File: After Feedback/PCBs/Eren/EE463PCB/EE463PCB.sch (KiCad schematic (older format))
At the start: 16 parts, among them J1 Conn_01x03, J2 Conn_01x02, Q1 IPD50R650CE, U1 HV9961LG-G

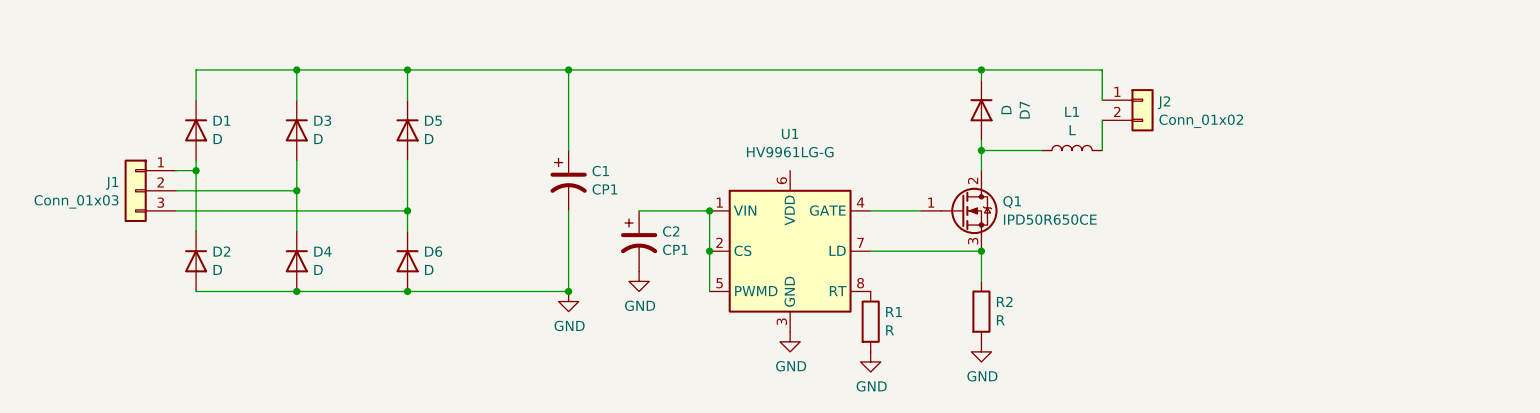
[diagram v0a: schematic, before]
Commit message: New components file is updated and PCB schematic is also updated
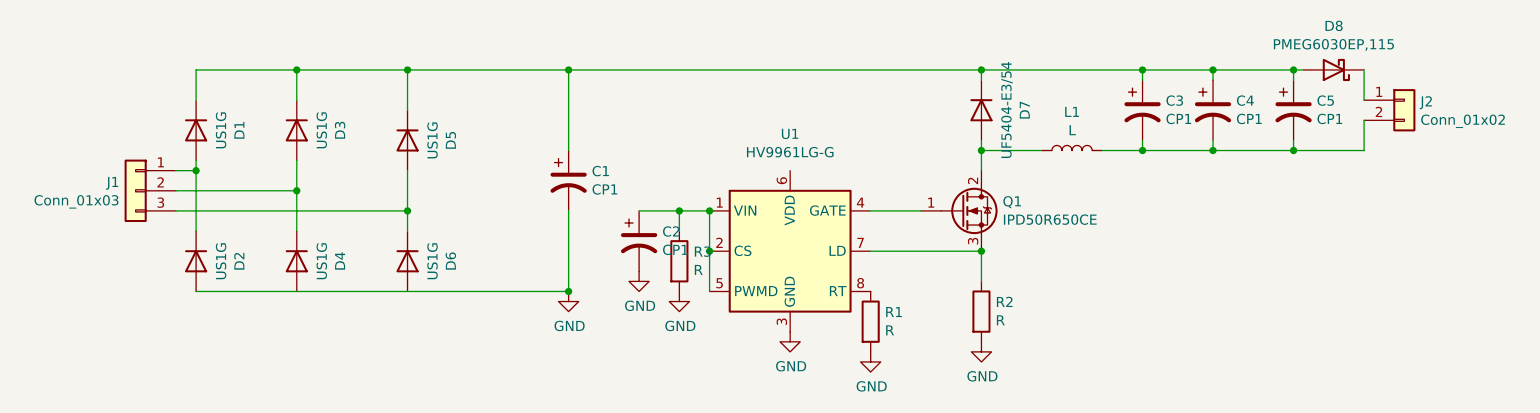
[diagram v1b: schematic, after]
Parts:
- removed D1, D2, D3, D4, D5, D6, D7: D, symbol Device:D
- added C3, C4, C5: CP1, Capacitor_SMD:C_0201_0603Metric, symbol Device:CP1
- added D1, D2, D3, D4, D5, D6: US1G, Diode_SMD:D_SMA, symbol Diode:US1G
- added D7: UF5404-E3/54, Diode_THT:D_DO-201AD_P15.24mm_Horizontal, symbol Diode:UF5404
- added D8: PMEG6030EP,115, Diode_SMD:D_SOD-128, symbol Diode:PMEG6030EP
- added R3: R, Resistor_SMD:R_4020_10251Metric, symbol Device:R
- C1: footprint (none) -> Capacitor_THT:CP_Axial_L25.0mm_D10.0mm_P30.00mm_Horizontal
- C2: footprint (none) -> Capacitor_SMD:C_0402_1005Metric
- J1: footprint (none) -> Connector_PinSocket_2.54mm:PinSocket_1x03_P2.54mm_Vertical
- J2: footprint (none) -> Connector_PinSocket_1.00mm:PinSocket_1x02_P1.00mm_Vertical
- L1: footprint (none) -> Inductor_THT:L_Radial_D28.0mm_P29.20mm
- R1, R2: footprint (none) -> Resistor_SMD:R_4020_10251Metric
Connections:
- net GND: now also D2.2 (A), R3.2
- net at C2.1, U1.1 (VIN), U1.2 (CS)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: now also R3.1
- net at J2.1 (Pin_1): now also D8.1 (K); no longer C1.1
- net at J2.2 (Pin_2), L1.2: now also C3.2, C4.2, C5.2
- net at J1.3 (Pin_3): now also D5.2 (A), D6.1 (K)
- net at J1.2 (Pin_2): now also D3.2 (A), D4.1 (K)
- net at J1.1 (Pin_1): now also D1.2 (A), D2.1 (K)
- net at L1.1, Q1.2 (D): now also D7.2 (A)
- new net: C1.1, C3.1, C4.1, C5.1, D1.1 (K), D3.1 (K), D5.1 (K), D7.1 (K), D8.2 (A)
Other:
- moved on the sheet: J2
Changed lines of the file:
@@
 F 0 "R1" H 6920 4746 50  0000 L CNN
 F 1 "R" H 6920 4655 50  0000 L CNN
-F 2 "" V 6780 4700 50  0001 C CNN
+F 2 "Resistor_SMD:R_4020_10251Metric" V 6780 4700 50  0001 C CNN
 F 3 "~" H 6850 4700 50  0001 C CNN
 	1    6850 4700
@@
 F 0 "R2" H 7470 4696 50  0000 L CNN
 F 1 "R" H 7470 4605 50  0000 L CNN
-F 2 "" V 7330 4650 50  0001 C CNN
+F 2 "Resistor_SMD:R_4020_10251Metric" V 7330 4650 50  0001 C CNN
 F 3 "~" H 7400 4650 50  0001 C CNN
 	1    7400 4650
@@
 F 0 "C2" H 5815 4346 50  0000 L CNN
 F 1 "CP1" H 5815 4255 50  0000 L CNN
-F 2 "" H 5700 4300 50  0001 C CNN
+F 2 "Capacitor_SMD:C_0402_1005Metric" H 5700 4300 50  0001 C CNN
 F 3 "~" H 5700 4300 50  0001 C CNN
 	1    5700 4300
@@
 Connection ~ 6050 4350
 Wire Wire Line
-	6050 4150 5700 4150
+	6050 4150 5900 4150
 Connection ~ 6050 4150
-$Comp
-L Device:D D7
-U 1 1 5FF92910
-P 7400 3650
-F 0 "D7" H 7400 3867 50  0000 C CNN
-F 1 "D" H 7400 3776 50  0000 C CNN
-F 2 "" H 7400 3650 50  0001 C CNN
-F 3 "~" H 7400 3650 50  0001 C CNN
-	1    7400 3650
-	0    1    1    0
-$EndComp
 Wire Wire Line
 	7400 3950 7400 3850
@@
 F 0 "L1" V 8040 3850 50  0000 C CNN
 F 1 "L" V 7949 3850 50  0000 C CNN
-F 2 "" H 7850 3850 50  0001 C CNN
+F 2 "Inductor_THT:L_Radial_D28.0mm_P29.20mm" H 7850 3850 50  0001 C CNN
 F 3 "~" H 7850 3850 50  0001 C CNN
 	1    7850 3850
@@
 F 0 "C1" H 5465 4046 50  0000 L CNN
 F 1 "CP1" H 5465 3955 50  0000 L CNN
-F 2 "" H 5350 4000 50  0001 C CNN
+F 2 "Capacitor_THT:CP_Axial_L25.0mm_D10.0mm_P30.00mm_Horizontal" H 5350 4000 50  0001 C CNN
 F 3 "~" H 5350 4000 50  0001 C CNN
 	1    5350 4000
@@
 Wire Wire Line
 	7400 3850 7400 3800
-Wire Wire Line
-	7400 3450 8000 3450
-Connection ~ 7400 3450
 $Comp
 L Connector_Generic:Conn_01x02 J2
 U 1 1 5FF87428
-P 8200 3600
-F 0 "J2" H 8280 3592 50  0000 L CNN
-F 1 "Conn_01x02" H 8280 3501 50  0000 L CNN
-F 2 "" H 8200 3600 50  0001 C CNN
-F 3 "~" H 8200 3600 50  0001 C CNN
-	1    8200 3600
-	1    0    0    -1
-$EndComp
-Wire Wire Line
-	8000 3850 8000 3700
-Wire Wire Line
-	8000 3450 8000 3600
-$Comp
-L Device:D D5
-U 1 1 5FF893A3
-P 4550 3750
-F 0 "D5" V 4504 3830 50  0000 L CNN
-F 1 "D" V 4595 3830 50  0000 L CNN
-F 2 "" H 4550 3750 50  0001 C CNN
-F 3 "~" H 4550 3750 50  0001 C CNN
-	1    4550 3750
-	0    1    1    0
-$EndComp
-$Comp
-L Device:D D3
-U 1 1 5FF8B368
-P 4000 3750
-F 0 "D3" V 3954 3830 50  0000 L CNN
-F 1 "D" V 4045 3830 50  0000 L CNN
-F 2 "" H 4000 3750 50  0001 C CNN
-F 3 "~" H 4000 3750 50  0001 C CNN
-	1    4000 3750
-	0    1    1    0
-$EndComp
-$Comp
-L Device:D D1
-U 1 1 5FF8B8EB
-P 3500 3750
-F 0 "D1" V 3454 3830 50  0000 L CNN
-F 1 "D" V 3545 3830 50  0000 L CNN
-F 2 "" H 3500 3750 50  0001 C CNN
-F 3 "~" H 3500 3750 50  0001 C CNN
-	1    3500 3750
-	0    1    1    0
-$EndComp
-$Comp
-L Device:D D6
-U 1 1 5FF8D494
-P 4550 4400
-F 0 "D6" V 4504 4480 50  0000 L CNN
-F 1 "D" V 4595 4480 50  0000 L CNN
-F 2 "" H 4550 4400 50  0001 C CNN
-F 3 "~" H 4550 4400 50  0001 C CNN
-	1    4550 4400
-	0    1    1    0
-$EndComp
-$Comp
-L Device:D D4
-U 1 1 5FF8D49A
-P 4000 4400
-F 0 "D4" V 3954 4480 50  0000 L CNN
-F 1 "D" V 4045 4480 50  0000 L CNN
-F 2 "" H 4000 4400 50  0001 C CNN
-F 3 "~" H 4000 4400 50  0001 C CNN
-	1    4000 4400
-	0    1    1    0
-$EndComp
-$Comp
-L Device:D D2
-U 1 1 5FF8D4A0
-P 3500 4400
-F 0 "D2" V 3454 4480 50  0000 L CNN
-F 1 "D" V 3545 4480 50  0000 L CNN
-F 2 "" H 3500 4400 50  0001 C CNN
-F 3 "~" H 3500 4400 50  0001 C CNN
-	1    3500 4400
-	0    1    1    0
+P 9500 3600
+F 0 "J2" H 9580 3592 50  0000 L CNN
+F 1 "Conn_01x02" H 9580 3501 50  0000 L CNN
+F 2 "Connector_PinSocket_1.00mm:PinSocket_1x02_P1.00mm_Vertical" H 9500 3600 50  0001 C CNN
+F 3 "~" H 9500 3600 50  0001 C CNN
+	1    9500 3600
+	1    0    0    -1
 $EndComp
 Wire Wire Line
@@
 Wire Wire Line
 	5350 3450 4550 3450
-Wire Wire Line
-	4550 3450 4550 3600
 Connection ~ 5350 3450
-Wire Wire Line
-	4550 3450 4000 3450
-Wire Wire Line
-	4000 3450 4000 3600
 Connection ~ 4550 3450
 Wire Wire Line
-	4000 3450 3500 3450
-Wire Wire Line
 	3500 3450 3500 3600
-Connection ~ 4000 3450
 Wire Wire Line
 	3500 4250 3500 3950
 Wire Wire Line
-	3500 4550 4000 4550
-Wire Wire Line
-	4000 4550 4550 4550
-Connection ~ 4000 4550
-Wire Wire Line
-	4550 4550 5350 4550
-Wire Wire Line
 	5350 4550 5350 4150
-Connection ~ 4550 4550
 $Comp
 L Connector_Generic:Conn_01x03 J1
@@
 F 0 "J1" H 3280 4092 50  0000 L CNN
 F 1 "Conn_01x03" H 3280 4001 50  0000 L CNN
-F 2 "" H 3200 4050 50  0001 C CNN
+F 2 "Connector_PinSocket_2.54mm:PinSocket_1x03_P2.54mm_Vertical" H 3200 4050 50  0001 C CNN
 F 3 "~" H 3200 4050 50  0001 C CNN
 	1    3200 4050
@@
 	4000 4050 4000 4250
 Wire Wire Line
-	4550 3900 4550 4150
-Wire Wire Line
 	3400 4150 4550 4150
-Connection ~ 4550 4150
 Wire Wire Line
 	4550 4150 4550 4250
@@
 $EndComp
 Connection ~ 5350 4550
+$Comp
+L Device:R R3
+U 1 1 5FF9D255
+P 5900 4400
+F 0 "R3" H 5970 4446 50  0000 L CNN
+F 1 "R" H 5970 4355 50  0000 L CNN
+F 2 "Resistor_SMD:R_4020_10251Metric" V 5830 4400 50  0001 C CNN
+F 3 "~" H 5900 4400 50  0001 C CNN
+	1    5900 4400
+	1    0    0    -1
+$EndComp
+Wire Wire Line
+	5900 4250 5900 4150
+Connection ~ 5900 4150
+Wire Wire Line
+	5900 4150 5700 4150
+$Comp
+L power:GND #PWR06
+U 1 1 5FF9E138
+P 5900 4550
+F 0 "#PWR06" H 5900 4300 50  0001 C CNN
+F 1 "GND" H 5905 4377 50  0000 C CNN
+F 2 "" H 5900 4550 50  0001 C CNN
+F 3 "" H 5900 4550 50  0001 C CNN
+	1    5900 4550
+	1    0    0    -1
+$EndComp
+$Comp
+L Device:CP1 C3
+U 1 1 5FFA0F5C
+P 8200 3650
+F 0 "C3" H 8315 3696 50  0000 L CNN
+F 1 "CP1" H 8315 3605 50  0000 L CNN
+F 2 "Capacitor_SMD:C_0201_0603Metric" H 8200 3650 50  0001 C CNN
+F 3 "~" H 8200 3650 50  0001 C CNN
+	1    8200 3650
+	1    0    0    -1
+$EndComp
+Wire Wire Line
+	8200 3450 8200 3500
+Wire Wire Line
+	8200 3800 8200 3850
+Wire Wire Line
+	8200 3850 8000 3850
+Connection ~ 8200 3850
+$Comp
+L Device:CP1 C4
+U 1 1 5FFB0889
+P 8550 3650
+F 0 "C4" H 8665 3696 50  0000 L CNN
+F 1 "CP1" H 8665 3605 50  0000 L CNN
+F 2 "Capacitor_SMD:C_0201_0603Metric" H 8550 3650 50  0001 C CNN
+F 3 "~" H 8550 3650 50  0001 C CNN
+	1    8550 3650
+	1    0    0    -1
+$EndComp
+$Comp
+L Device:CP1 C5
+U 1 1 5FFB13E8
+P 8950 3650
+F 0 "C5" H 9065 3696 50  0000 L CNN
+F 1 "CP1" H 9065 3605 50  0000 L CNN
+F 2 "Capacitor_SMD:C_0201_0603Metric" H 8950 3650 50  0001 C CNN
+F 3 "~" H 8950 3650 50  0001 C CNN
+	1    8950 3650
+	1    0    0    -1
+$EndComp
+Wire Wire Line
+	8550 3450 8550 3500
+Wire Wire Line
+	8200 3450 8550 3450
+Wire Wire Line
+	8550 3450 8950 3450
+Wire Wire Line
+	8950 3450 8950 3500
+Connection ~ 8550 3450
+Wire Wire Line
+	8550 3800 8550 3850
+Wire Wire Line
+	8200 3850 8550 3850
+Wire Wire Line
+	8950 3800 8950 3850
+Wire Wire Line
+	8950 3850 8550 3850
+Connection ~ 8550 3850
+Wire Wire Line
+	9300 3700 9300 3850
+Wire Wire Line
+	9300 3850 8950 3850
+Connection ~ 8950 3850
+$Comp
+L Diode:US1G D1
+U 1 1 5FFBE7C3
+P 3500 3750
+F 0 "D1" H 3500 3967 50  0000 C CNN
+F 1 "US1G" H 3500 3876 50  0000 C CNN
+F 2 "Diode_SMD:D_SMA" H 3500 3575 50  0001 C CNN
+F 3 "https://www.diodes.com/assets/Datasheets/ds16008.pdf" H 3500 3750 50  0001 C CNN
+	1    3500 3750
+	0    1    1    0
+$EndComp
+Wire Wire Line
+	3500 3450 4000 3450
+Wire Wire Line
+	3500 4550 5350 4550
+$Comp
+L Diode:US1G D3
+U 1 1 5FFC5787
+P 4000 3750
+F 0 "D3" H 4000 3967 50  0000 C CNN
+F 1 "US1G" H 4000 3876 50  0000 C CNN
+F 2 "Diode_SMD:D_SMA" H 4000 3575 50  0001 C CNN
+F 3 "https://www.diodes.com/assets/Datasheets/ds16008.pdf" H 4000 3750 50  0001 C CNN
+	1    4000 3750
+	0    1    1    0
+$EndComp
+Wire Wire Line
+	4550 3450 4550 3650
+Wire Wire Line
+	4000 3600 4000 3450
+Connection ~ 4000 3450
+Wire Wire Line
+	4000 3450 4550 3450
+$Comp
+L Diode:US1G D5
+U 1 1 5FFCE750
+P 4550 3800
+F 0 "D5" H 4550 4017 50  0000 C CNN
+F 1 "US1G" H 4550 3926 50  0000 C CNN
+F 2 "Diode_SMD:D_SMA" H 4550 3625 50  0001 C CNN
+F 3 "https://www.diodes.com/assets/Datasheets/ds16008.pdf" H 4550 3800 50  0001 C CNN
+	1    4550 3800
+	0    1    1    0
+$EndComp
+$Comp
+L Diode:US1G D6
+U 1 1 5FFCF1AA
+P 4550 4400
+F 0 "D6" H 4550 4617 50  0000 C CNN
+F 1 "US1G" H 4550 4526 50  0000 C CNN
+F 2 "Diode_SMD:D_SMA" H 4550 4225 50  0001 C CNN
+F 3 "https://www.diodes.com/assets/Datasheets/ds16008.pdf" H 4550 4400 50  0001 C CNN
+	1    4550 4400
+	0    1    1    0
+$EndComp
+$Comp
+L Diode:US1G D4
+U 1 1 5FFCFBD4
+P 4000 4400
+F 0 "D4" H 4000 4617 50  0000 C CNN
+F 1 "US1G" H 4000 4526 50  0000 C CNN
+F 2 "Diode_SMD:D_SMA" H 4000 4225 50  0001 C CNN
+F 3 "https://www.diodes.com/assets/Datasheets/ds16008.pdf" H 4000 4400 50  0001 C CNN
+	1    4000 4400
+	0    1    1    0
+$EndComp
+$Comp
+L Diode:US1G D2
+U 1 1 5FFD08BC
+P 3500 4400
+F 0 "D2" H 3500 4617 50  0000 C CNN
+F 1 "US1G" H 3500 4526 50  0000 C CNN
+F 2 "Diode_SMD:D_SMA" H 3500 4225 50  0001 C CNN
+F 3 "https://www.diodes.com/assets/Datasheets/ds16008.pdf" H 3500 4400 50  0001 C CNN
+	1    3500 4400
+	0    1    1    0
+$EndComp
+Wire Wire Line
+	4550 4150 4550 3950
+Connection ~ 4550 4150
+Connection ~ 7400 3450
+Wire Wire Line
+	7400 3450 8200 3450
+Connection ~ 8200 3450
+Wire Wire Line
+	9000 3450 8950 3450
+Connection ~ 8950 3450
+$Comp
+L Diode:UF5404 D7
+U 1 1 5FFDD25C
+P 7400 3650
+F 0 "D7" H 7400 3867 50  0000 C CNN
+F 1 "UF5404-E3/54" H 7400 3776 50  0000 C CNN
+F 2 "Diode_THT:D_DO-201AD_P15.24mm_Horizontal" H 7400 3475 50  0001 C CNN
+F 3 "http://www.vishay.com/docs/88756/uf5400.pdf" H 7400 3650 50  0001 C CNN
+	1    7400 3650
+	0    1    1    0
+$EndComp
+$Comp
+L Diode:PMEG6030EP D8
+U 1 1 5FFE3A52
+P 9150 3450
+F 0 "D8" H 9150 3233 50  0000 C CNN
+F 1 "PMEG6030EP,115" H 9150 3324 50  0000 C CNN
+F 2 "Diode_SMD:D_SOD-128" H 9150 3275 50  0001 C CNN
+F 3 "https://assets.nexperia.com/documents/data-sheet/PMEG6030EP.pdf" H 9150 3450 50  0001 C CNN
+	1    9150 3450
+	-1   0    0    1
+$EndComp
+Wire Wire Line
+	9300 3600 9300 3450
 $EndSCHEMATC
